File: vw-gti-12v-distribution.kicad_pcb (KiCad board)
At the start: 2 copper layers, 90 x 75 mm, 4 parts, among them J1 IN_12V, J2 OUT_DASHCAM, J3 OUT_PHONE, J4 OUT_BOOST

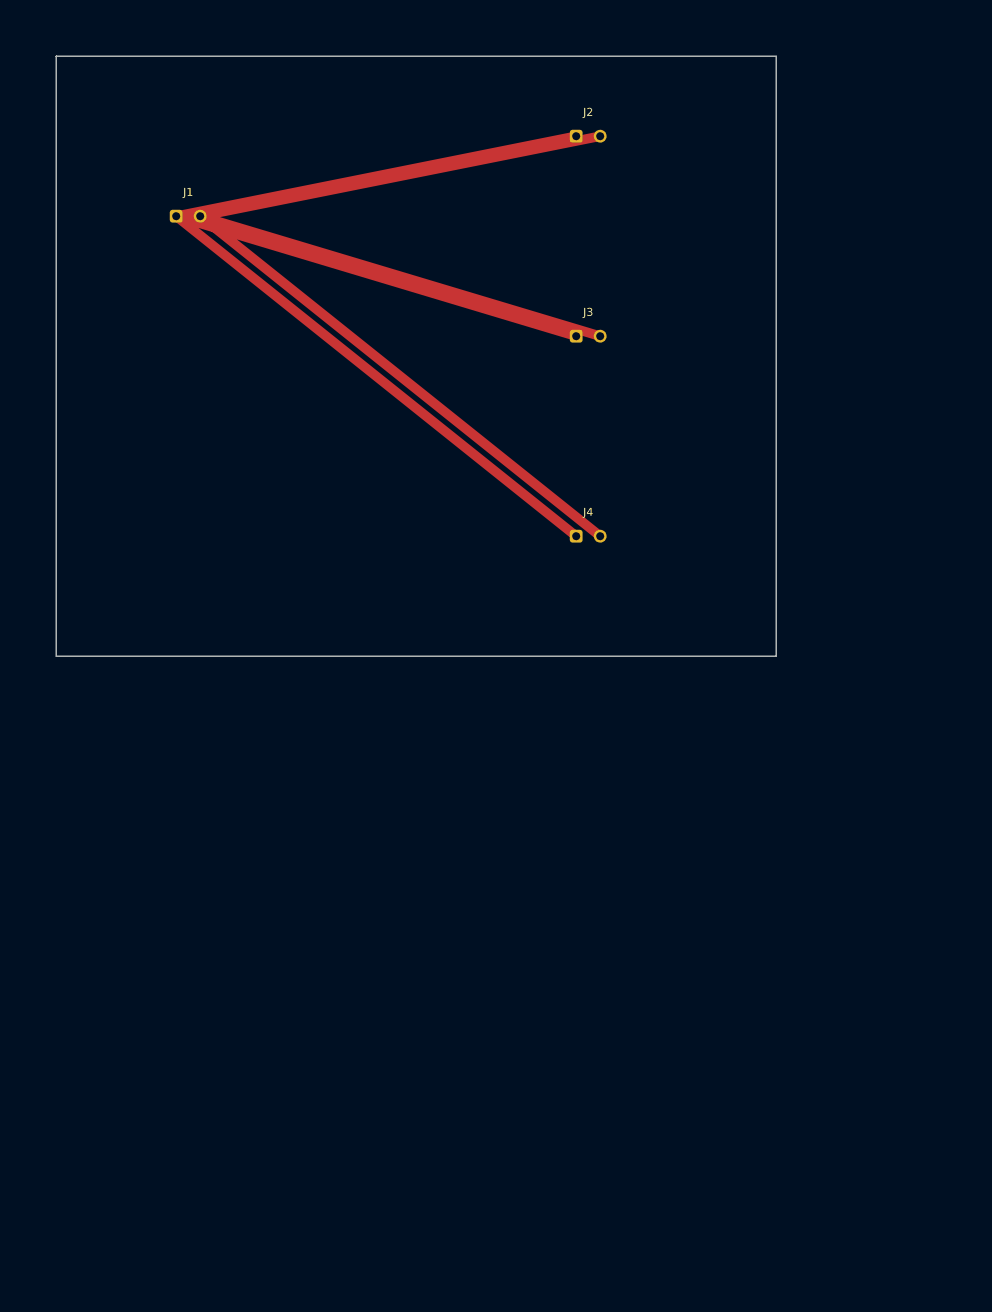
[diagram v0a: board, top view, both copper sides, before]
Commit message: Switch to SMD PicoSpoX and add ACC + extra outputs
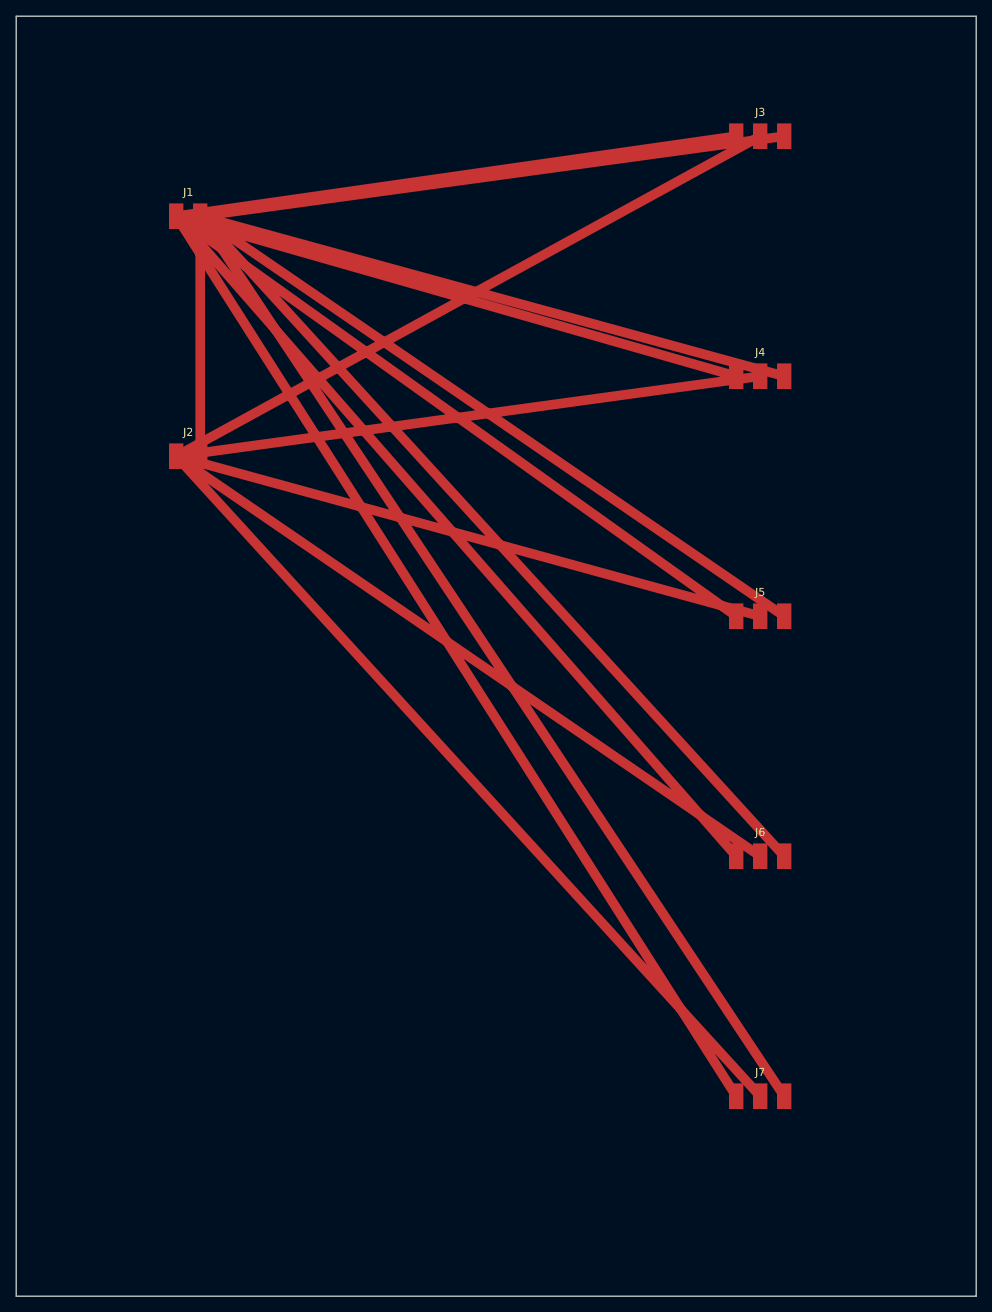
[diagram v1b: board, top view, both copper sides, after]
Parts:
- added J5: OUT_BOOST, PicoSpoX:PicoSpoX_1x03_P3.00mm_SMD, F.Cu at (110.0, 90.0)
- added J6: OUT_SPARE1, PicoSpoX:PicoSpoX_1x03_P3.00mm_SMD, F.Cu at (110.0, 120.0)
- added J7: OUT_SPARE2, PicoSpoX:PicoSpoX_1x03_P3.00mm_SMD, F.Cu at (110.0, 150.0)
- J1: value IN_12V -> IN_BATT; footprint PicoSpoX:PicoSpoX_1x02_P3.00mm_THT -> PicoSpoX:PicoSpoX_1x02_P3.00mm_SMD
- J2: value OUT_DASHCAM -> IN_ACC; footprint PicoSpoX:PicoSpoX_1x02_P3.00mm_THT -> PicoSpoX:PicoSpoX_1x02_P3.00mm_SMD
- J3: value OUT_PHONE -> OUT_DASHCAM; footprint PicoSpoX:PicoSpoX_1x02_P3.00mm_THT -> PicoSpoX:PicoSpoX_1x03_P3.00mm_SMD
- J4: value OUT_BOOST -> OUT_PHONE; footprint PicoSpoX:PicoSpoX_1x02_P3.00mm_THT -> PicoSpoX:PicoSpoX_1x03_P3.00mm_SMD
- moved J2 64.0 mm to (40.0, 70.0)
- moved J3 32.0 mm to (110.0, 30.0)
- moved J4 28.3 mm to (110.0, 60.0)
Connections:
- J1 pad 1: +12V -> +12V_BATT
- J2 pad 1: +12V -> +12V_ACC
- J3 pad 1: +12V -> +12V_BATT
- J3 pad 2: GND -> +12V_ACC
- J4 pad 1: +12V -> +12V_BATT
- J4 pad 2: GND -> +12V_ACC
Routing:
- net +12V_BATT: track 0.00 -> 466.2 mm
- net +12V_ACC: track 0.00 -> 429.4 mm
- net GND: track 167.2 -> 508.2 mm
- net +12V: track 167.2 -> 0.00 mm
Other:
- board size 90 x 75 mm -> 120 x 160 mm
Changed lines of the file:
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@@
   (net 0 "")
   (net 1 "GND")
-  (net 2 "+12V")
-  (footprint "PicoSpoX:PicoSpoX_1x02_P3.00mm_THT" (layer "F.Cu")
+  (net 2 "+12V_BATT")
+  (net 3 "+12V_ACC")
+  (footprint "PicoSpoX:PicoSpoX_1x02_P3.00mm_SMD" (layer "F.Cu")
     (at 40 40)
     (property "Reference" "J1" (at 1.5 -3) (layer "F.SilkS") (effects (font (size 1 1) (thickness 0.15))))
-    (property "Value" "IN_12V" (at 1.5 3) (layer "F.Fab") (effects (font (size 1 1) (thickness 0.15))))
-    (pad "1" thru_hole roundrect (at 0 0) (size 1.6 1.6) (drill 1.0) (layers "*.Cu" "*.Mask") (roundrect_rratio 0.2) (net 2))
-    (pad "2" thru_hole circle (at 3 0) (size 1.6 1.6) (drill 1.0) (layers "*.Cu" "*.Mask") (net 1))
+    (property "Value" "IN_BATT" (at 1.5 3) (layer "F.Fab") (effects (font (size 1 1) (thickness 0.15))))
+    (pad "1" smd rect (at 0 0) (size 1.8 3.2) (layers "F.Cu" "F.Paste" "F.Mask") (net 2))
+    (pad "2" smd rect (at 3 0) (size 1.8 3.2) (layers "F.Cu" "F.Paste" "F.Mask") (net 1))
   )
-  (footprint "PicoSpoX:PicoSpoX_1x02_P3.00mm_THT" (layer "F.Cu")
-    (at 90 30)
+  (footprint "PicoSpoX:PicoSpoX_1x02_P3.00mm_SMD" (layer "F.Cu")
+    (at 40 70)
     (property "Reference" "J2" (at 1.5 -3) (layer "F.SilkS") (effects (font (size 1 1) (thickness 0.15))))
-    (property "Value" "OUT_DASHCAM" (at 1.5 3) (layer "F.Fab") (effects (font (size 1 1) (thickness 0.15))))
-    (pad "1" thru_hole roundrect (at 0 0) (size 1.6 1.6) (drill 1.0) (layers "*.Cu" "*.Mask") (roundrect_rratio 0.2) (net 2))
-    (pad "2" thru_hole circle (at 3 0) (size 1.6 1.6) (drill 1.0) (layers "*.Cu" "*.Mask") (net 1))
+    (property "Value" "IN_ACC" (at 1.5 3) (layer "F.Fab") (effects (font (size 1 1) (thickness 0.15))))
+    (pad "1" smd rect (at 0 0) (size 1.8 3.2) (layers "F.Cu" "F.Paste" "F.Mask") (net 3))
+    (pad "2" smd rect (at 3 0) (size 1.8 3.2) (layers "F.Cu" "F.Paste" "F.Mask") (net 1))
   )
-  (footprint "PicoSpoX:PicoSpoX_1x02_P3.00mm_THT" (layer "F.Cu")
-    (at 90 55)
-    (property "Reference" "J3" (at 1.5 -3) (layer "F.SilkS") (effects (font (size 1 1) (thickness 0.15))))
-    (property "Value" "OUT_PHONE" (at 1.5 3) (layer "F.Fab") (effects (font (size 1 1) (thickness 0.15))))
-    (pad "1" thru_hole roundrect (at 0 0) (size 1.6 1.6) (drill 1.0) (layers "*.Cu" "*.Mask") (roundrect_rratio 0.2) (net 2))
-    (pad "2" thru_hole circle (at 3 0) (size 1.6 1.6) (drill 1.0) (layers "*.Cu" "*.Mask") (net 1))
+  (footprint "PicoSpoX:PicoSpoX_1x03_P3.00mm_SMD" (layer "F.Cu")
+    (at 110 30)
+    (property "Reference" "J3" (at 3 -3) (layer "F.SilkS") (effects (font (size 1 1) (thickness 0.15))))
+    (property "Value" "OUT_DASHCAM" (at 3 3) (layer "F.Fab") (effects (font (size 1 1) (thickness 0.15))))
+    (pad "1" smd rect (at 0 0) (size 1.8 3.2) (layers "F.Cu" "F.Paste" "F.Mask") (net 2))
+    (pad "2" smd rect (at 3 0) (size 1.8 3.2) (layers "F.Cu" "F.Paste" "F.Mask") (net 3))
+    (pad "3" smd rect (at 6 0) (size 1.8 3.2) (layers "F.Cu" "F.Paste" "F.Mask") (net 1))
   )
-  (footprint "PicoSpoX:PicoSpoX_1x02_P3.00mm_THT" (layer "F.Cu")
-    (at 90 80)
-    (property "Reference" "J4" (at 1.5 -3) (layer "F.SilkS") (effects (font (size 1 1) (thickness 0.15))))
-    (property "Value" "OUT_BOOST" (at 1.5 3) (layer "F.Fab") (effects (font (size 1 1) (thickness 0.15))))
-    (pad "1" thru_hole roundrect (at 0 0) (size 1.6 1.6) (drill 1.0) (layers "*.Cu" "*.Mask") (roundrect_rratio 0.2) (net 2))
-    (pad "2" thru_hole circle (at 3 0) (size 1.6 1.6) (drill 1.0) (layers "*.Cu" "*.Mask") (net 1))
+  (footprint "PicoSpoX:PicoSpoX_1x03_P3.00mm_SMD" (layer "F.Cu")
+    (at 110 60)
+    (property "Reference" "J4" (at 3 -3) (layer "F.SilkS") (effects (font (size 1 1) (thickness 0.15))))
+    (property "Value" "OUT_PHONE" (at 3 3) (layer "F.Fab") (effects (font (size 1 1) (thickness 0.15))))
+    (pad "1" smd rect (at 0 0) (size 1.8 3.2) (layers "F.Cu" "F.Paste" "F.Mask") (net 2))
+    (pad "2" smd rect (at 3 0) (size 1.8 3.2) (layers "F.Cu" "F.Paste" "F.Mask") (net 3))
+    (pad "3" smd rect (at 6 0) (size 1.8 3.2) (layers "F.Cu" "F.Paste" "F.Mask") (net 1))
   )
-  (gr_rect (start 25 20) (end 115 95) (layer "Edge.Cuts") (width 0.05))
-  (segment (start 40 40) (end 90 30) (width 1.2) (layer "F.Cu") (net 2))
-  (segment (start 40 40) (end 90 55) (width 1.2) (layer "F.Cu") (net 2))
-  (segment (start 40 40) (end 90 80) (width 1.2) (layer "F.Cu") (net 2))
-  (segment (start 43 40) (end 93 30) (width 1.2) (layer "F.Cu") (net 1))
-  (segment (start 43 40) (end 93 55) (width 1.2) (layer "F.Cu") (net 1))
-  (segment (start 43 40) (end 93 80) (width 1.2) (layer "F.Cu") (net 1))
+  (footprint "PicoSpoX:PicoSpoX_1x03_P3.00mm_SMD" (layer "F.Cu")
+    (at 110 90)
+    (property "Reference" "J5" (at 3 -3) (layer "F.SilkS") (effects (font (size 1 1) (thickness 0.15))))
+    (property "Value" "OUT_BOOST" (at 3 3) (layer "F.Fab") (effects (font (size 1 1) (thickness 0.15))))
+    (pad "1" smd rect (at 0 0) (size 1.8 3.2) (layers "F.Cu" "F.Paste" "F.Mask") (net 2))
+    (pad "2" smd rect (at 3 0) (size 1.8 3.2) (layers "F.Cu" "F.Paste" "F.Mask") (net 3))
+    (pad "3" smd rect (at 6 0) (size 1.8 3.2) (layers "F.Cu" "F.Paste" "F.Mask") (net 1))
+  )
+  (footprint "PicoSpoX:PicoSpoX_1x03_P3.00mm_SMD" (layer "F.Cu")
+    (at 110 120)
+    (property "Reference" "J6" (at 3 -3) (layer "F.SilkS") (effects (font (size 1 1) (thickness 0.15))))
+    (property "Value" "OUT_SPARE1" (at 3 3) (layer "F.Fab") (effects (font (size 1 1) (thickness 0.15))))
+    (pad "1" smd rect (at 0 0) (size 1.8 3.2) (layers "F.Cu" "F.Paste" "F.Mask") (net 2))
+    (pad "2" smd rect (at 3 0) (size 1.8 3.2) (layers "F.Cu" "F.Paste" "F.Mask") (net 3))
+    (pad "3" smd rect (at 6 0) (size 1.8 3.2) (layers "F.Cu" "F.Paste" "F.Mask") (net 1))
+  )
+  (footprint "PicoSpoX:PicoSpoX_1x03_P3.00mm_SMD" (layer "F.Cu")
+    (at 110 150)
+    (property "Reference" "J7" (at 3 -3) (layer "F.SilkS") (effects (font (size 1 1) (thickness 0.15))))
+    (property "Value" "OUT_SPARE2" (at 3 3) (layer "F.Fab") (effects (font (size 1 1) (thickness 0.15))))
+    (pad "1" smd rect (at 0 0) (size 1.8 3.2) (layers "F.Cu" "F.Paste" "F.Mask") (net 2))
+    (pad "2" smd rect (at 3 0) (size 1.8 3.2) (layers "F.Cu" "F.Paste" "F.Mask") (net 3))
+    (pad "3" smd rect (at 6 0) (size 1.8 3.2) (layers "F.Cu" "F.Paste" "F.Mask") (net 1))
+  )
+  (gr_rect (start 20 15) (end 140 175) (layer "Edge.Cuts") (width 0.05))
+  (segment (start 40 40) (end 110 30) (width 1.2) (layer "F.Cu") (net 2))
+  (segment (start 40 40) (end 110 60) (width 1.2) (layer "F.Cu") (net 2))
+  (segment (start 40 40) (end 110 90) (width 1.2) (layer "F.Cu") (net 2))
+  (segment (start 40 40) (end 110 120) (width 1.2) (layer "F.Cu") (net 2))
+  (segment (start 40 40) (end 110 150) (width 1.2) (layer "F.Cu") (net 2))
+  (segment (start 40 70) (end 113 30) (width 1.2) (layer "F.Cu") (net 3))
+  (segment (start 40 70) (end 113 60) (width 1.2) (layer "F.Cu") (net 3))
+  (segment (start 40 70) (end 113 90) (width 1.2) (layer "F.Cu") (net 3))
+  (segment (start 40 70) (end 113 120) (width 1.2) (layer "F.Cu") (net 3))
+  (segment (start 40 70) (end 113 150) (width 1.2) (layer "F.Cu") (net 3))
+  (segment (start 43 40) (end 43 70) (width 1.2) (layer "F.Cu") (net 1))
+  (segment (start 43 40) (end 116 30) (width 1.2) (layer "F.Cu") (net 1))
+  (segment (start 43 40) (end 116 60) (width 1.2) (layer "F.Cu") (net 1))
+  (segment (start 43 40) (end 116 90) (width 1.2) (layer "F.Cu") (net 1))
+  (segment (start 43 40) (end 116 120) (width 1.2) (layer "F.Cu") (net 1))
+  (segment (start 43 40) (end 116 150) (width 1.2) (layer "F.Cu") (net 1))
 )
